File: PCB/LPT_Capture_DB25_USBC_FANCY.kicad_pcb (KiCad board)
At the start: 2 copper layers, 36 x 22.8 mm, 23 parts, among them J1 GSB1C4621DS2HR, J2 DB25P064TXLF, Q1 SL2301S, Q2 SL2301S, U1 FT245RL

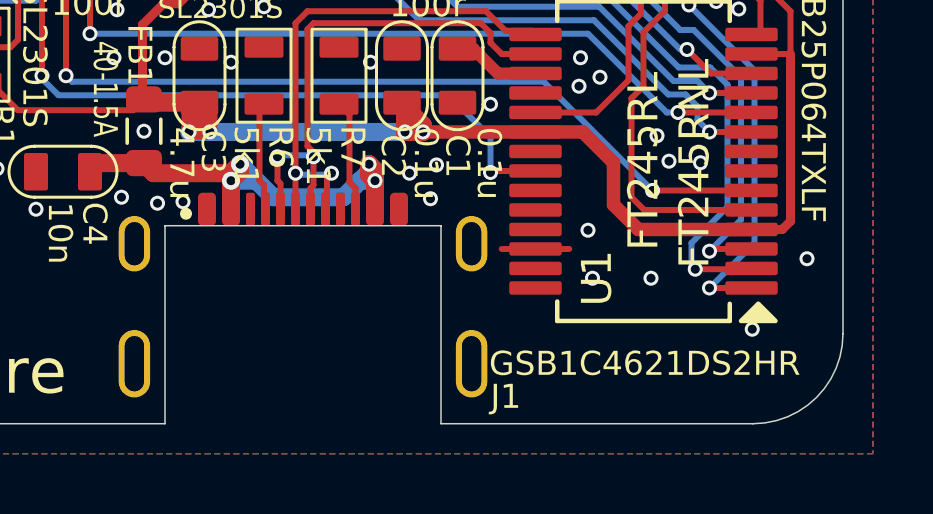
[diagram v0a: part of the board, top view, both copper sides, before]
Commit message: pull c36_usbc_fancy into main
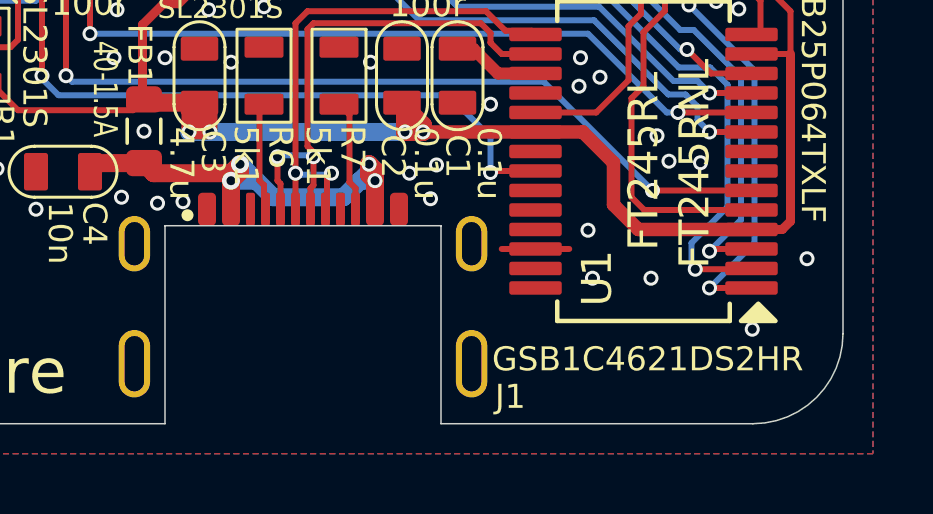
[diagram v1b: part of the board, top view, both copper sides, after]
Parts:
- J1: footprint 000_LOCAL:USBC_16pin_mid_mount -> 000_LOCAL:USBC_Receptacle_16pin_mid_mount
